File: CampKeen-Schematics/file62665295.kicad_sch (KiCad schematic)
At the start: 31 parts, among them Q10 2N7000, Q11 IRF9Z34NPBF, Q12 2N7000, Q13 2N7000, Q14 2N7000, Q15 2N7000, Q59 LTV-847

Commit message: working on input protection.
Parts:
- added R?: 1M, Resistor_THT:R_Axial_DIN0207_L6.3mm_D2.5mm_P2.54mm_Vertical, symbol Device:R
- Q59: footprint DIP762W60P254L1984H450Q16N -> SamacSys_Parts:DIP762W60P254L1984H450Q16N
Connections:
- net FullIN: now also R?.2; no longer Q14.2 (G), R47.1
- new net: Q14.2 (G), R47.1, R?.1
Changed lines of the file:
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@@
   (junction (at 158.75 153.67) (diameter 0) (color 0 0 0 0)
   )
+  (junction (at 144.78 134.62) (diameter 0) (color 0 0 0 0)
+  )
   (junction (at 68.58 20.32) (diameter 0) (color 0 0 0 0)
   )
@@
   (junction (at 116.84 96.52) (diameter 0) (color 0 0 0 0)
   )
-  (junction (at 144.78 134.62) (diameter 0) (color 0 0 0 0)
-  )
   (junction (at 40.64 52.07) (diameter 0) (color 0 0 0 0)
   )
@@
     (stroke (width 0) (type default) (color 0 0 0 0))
   )
-  (wire (pts (xy 134.62 134.62) (xy 144.78 134.62))
-    (stroke (width 0) (type default) (color 0 0 0 0))
-  )
   (wire (pts (xy 53.34 46.99) (xy 53.34 52.07))
     (stroke (width 0) (type default) (color 0 0 0 0))
@@
     (stroke (width 0) (type default) (color 0 0 0 0))
   )
+  (wire (pts (xy 134.62 134.62) (xy 135.89 134.62))
+    (stroke (width 0) (type default) (color 0 0 0 0))
+  )
   (wire (pts (xy 246.38 41.91) (xy 237.49 41.91))
     (stroke (width 0) (type default) (color 0 0 0 0))
   )
   (wire (pts (xy 144.78 149.86) (xy 144.78 153.67))
+    (stroke (width 0) (type default) (color 0 0 0 0))
+  )
+  (wire (pts (xy 143.51 134.62) (xy 144.78 134.62))
     (stroke (width 0) (type default) (color 0 0 0 0))
   )
@@
     (property "Reference" "Q59" (id 0) (at 207.01 30.099 0))
     (property "Value" "LTV-847" (id 1) (at 207.01 32.4104 0))
-    (property "Footprint" "DIP762W60P254L1984H450Q16N" (id 2) (at 224.79 34.29 0)
+    (property "Footprint" "SamacSys_Parts:DIP762W60P254L1984H450Q16N" (id 2) (at 224.79 34.29 0)
       (effects (font (size 1.27 1.27)) (justify left) hide)
     )
@@
       (effects (font (size 1.27 1.27)) hide)
     )
+    (pin "1")
+    (pin "2")
+  )
+  (symbol (lib_id "Device:R") (at 139.7 134.62 270)
+    (in_bom yes) (on_board yes)
+    (property "Reference" "R?" (id 0) (at 140.8684 136.398 0)
+      (effects (font (size 1.27 1.27)) (justify left))
+    )
+    (property "Value" "1M" (id 1) (at 138.557 136.398 0)
+      (effects (font (size 1.27 1.27)) (justify left))
+    )
+    (property "Footprint" "Resistor_THT:R_Axial_DIN0207_L6.3mm_D2.5mm_P2.54mm_Vertical" (id 2) (at 139.7 132.842 90)
+      (effects (font (size 1.27 1.27)) hide)
+    )
+    (property "Datasheet" "~" (id 3) (at 139.7 134.62 0)
+      (effects (font (size 1.27 1.27)) hide)
+    )

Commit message: work in progress for a design.
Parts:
- added R?: 220, Resistor_THT:R_Axial_DIN0207_L6.3mm_D2.5mm_P2.54mm_Vertical, symbol Device:R
- R47: value 1M -> 5K
- R?: value 1M -> 470
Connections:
- net FullIN: now also D12.1 (K), R47.1
- net at Q14.3 (D): now also R?.2; no longer D12.1 (K)
- net at D12.2 (A): now also Q14.2 (G), R?.1; no longer Q59.8 (CATHODE_4)
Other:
- moved on the sheet: C22, D12, Q14, R47, R?

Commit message: wip with changed values and delete of redundant resistor in new design
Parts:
- removed R?: 220, Resistor_THT:R_Axial_DIN0207_L6.3mm_D2.5mm_P2.54mm_Vertical, symbol Device:R
- renumbered C20 to C16, C21 to C17, C22 to C18, C23 to C19, D9 to D3, D10 to D6, D11 to D7, D12 to D8, Q10 to Q2, Q11 to Q3, Q12 to Q4, Q13 to Q5, Q59 to Q58, Q14 to Q6, Q15 to Q7, R40 to R15, R41 to R16, R42 to R17, R43 to R18, R44 to R19, R45 to R20, R46 to R21, R47 to R22, R48 to R23, R49 to R24, R50 to R25, R77 to R70, R78 to R71, R122 to R72, R123 to R76, Z3 to Z1
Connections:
- net FullIN: no longer R22.1
- net at D8.2 (A), Q6.2 (G), R?.1: now also R22.1
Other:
- moved on the sheet: C18, R22

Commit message: wip removing the traces fixing the inputs
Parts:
- removed C16, C17, C19: 22nF, Capacitor_THT:C_Disc_D4.7mm_W2.5mm_P5.00mm, symbol Device:C
- removed D3, D6, D7: 1N4007, Diode_THT:D_DO-41_SOD81_P10.16mm_Horizontal, symbol Diode:1N4007
- removed Q4, Q5, Q7: 2N7000, Package_TO_SOT_THT:TO-92_Inline, symbol Transistor_FET:2N7000
- removed R18, R19, R23: 1M, Resistor_THT:R_Axial_DIN0207_L6.3mm_D2.5mm_P2.54mm_Vertical, symbol Device:R
- removed R20, R21, R24, R25: 330, Resistor_THT:R_Axial_DIN0207_L6.3mm_D2.5mm_P2.54mm_Vertical, symbol Device:R
- removed R70, R71, R72, R76: 22k, Resistor_THT:R_Axial_DIN0207_L6.3mm_D2.5mm_P2.54mm_Vertical, symbol Device:R
- added C? (x3): 22nF, Capacitor_THT:C_Disc_D4.7mm_W2.5mm_P5.00mm, symbol Device:C
- added D? (x3): 1N4007, Diode_THT:D_DO-41_SOD81_P10.16mm_Horizontal, symbol Diode:1N4007
- added Q? (x3): 2N7000, Package_TO_SOT_THT:TO-92_Inline, symbol Transistor_FET:2N7000
- added R? (x3): 5K, Resistor_THT:R_Axial_DIN0207_L6.3mm_D2.5mm_P2.54mm_Vertical, symbol Device:R
- added R? (x3): 470, Resistor_THT:R_Axial_DIN0207_L6.3mm_D2.5mm_P2.54mm_Vertical, symbol Device:R
- added RN?: EXB-38V331JV, EXB38V472JV, symbol Samac_Sys:EXB-38V331JV
- added RN?: EXB-38V223JV, EXB38V472JV, symbol Samac_Sys:EXB-38V223JV
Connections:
- net +5V: now also RN?.5, RN?.5, RN?.6, RN?.6, RN?.7, RN?.7, RN?.8, RN?.8
- net 1-2IN: now also C?.1, D?.1 (K), R?.2
- net 1-2OUT: now also RN?.2
- net 1-4IN: now also C?.1, D?.1 (K), R?.2
- net 1-4OUT: now also RN?.1
- net 3-4IN: now also C?.1, D?.1 (K), R?.2
- net 3-4OUT: now also RN?.3
- net FullOUT: now also RN?.4
- net GND: now also C?.2, C?.2, C?.2, Q?.1 (S), Q?.1 (S), Q?.1 (S), R?.2, R?.2, R?.2
- net at Q58.2 (CATHODE_1): now also Q?.3 (D)
- net at Q58.4 (CATHODE_2): now also Q?.3 (D)
- net at Q58.6 (CATHODE_3): now also Q?.3 (D)
- net at Q58.1 (ANODE_1): now also RN?.4
- net at Q58.3 (ANODE_2): now also RN?.3
- net at Q58.5 (ANODE_3): now also RN?.2
- net at Q58.7 (ANODE_4): now also RN?.1
- net at Q58.8 (CATHODE_4): now also Q6.3 (D)
- new net: D?.2 (A), Q?.2 (G), R?.1, R?.1 (x3)
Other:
- moved on the sheet: C18, D8, Q58, Q6, R22, R?

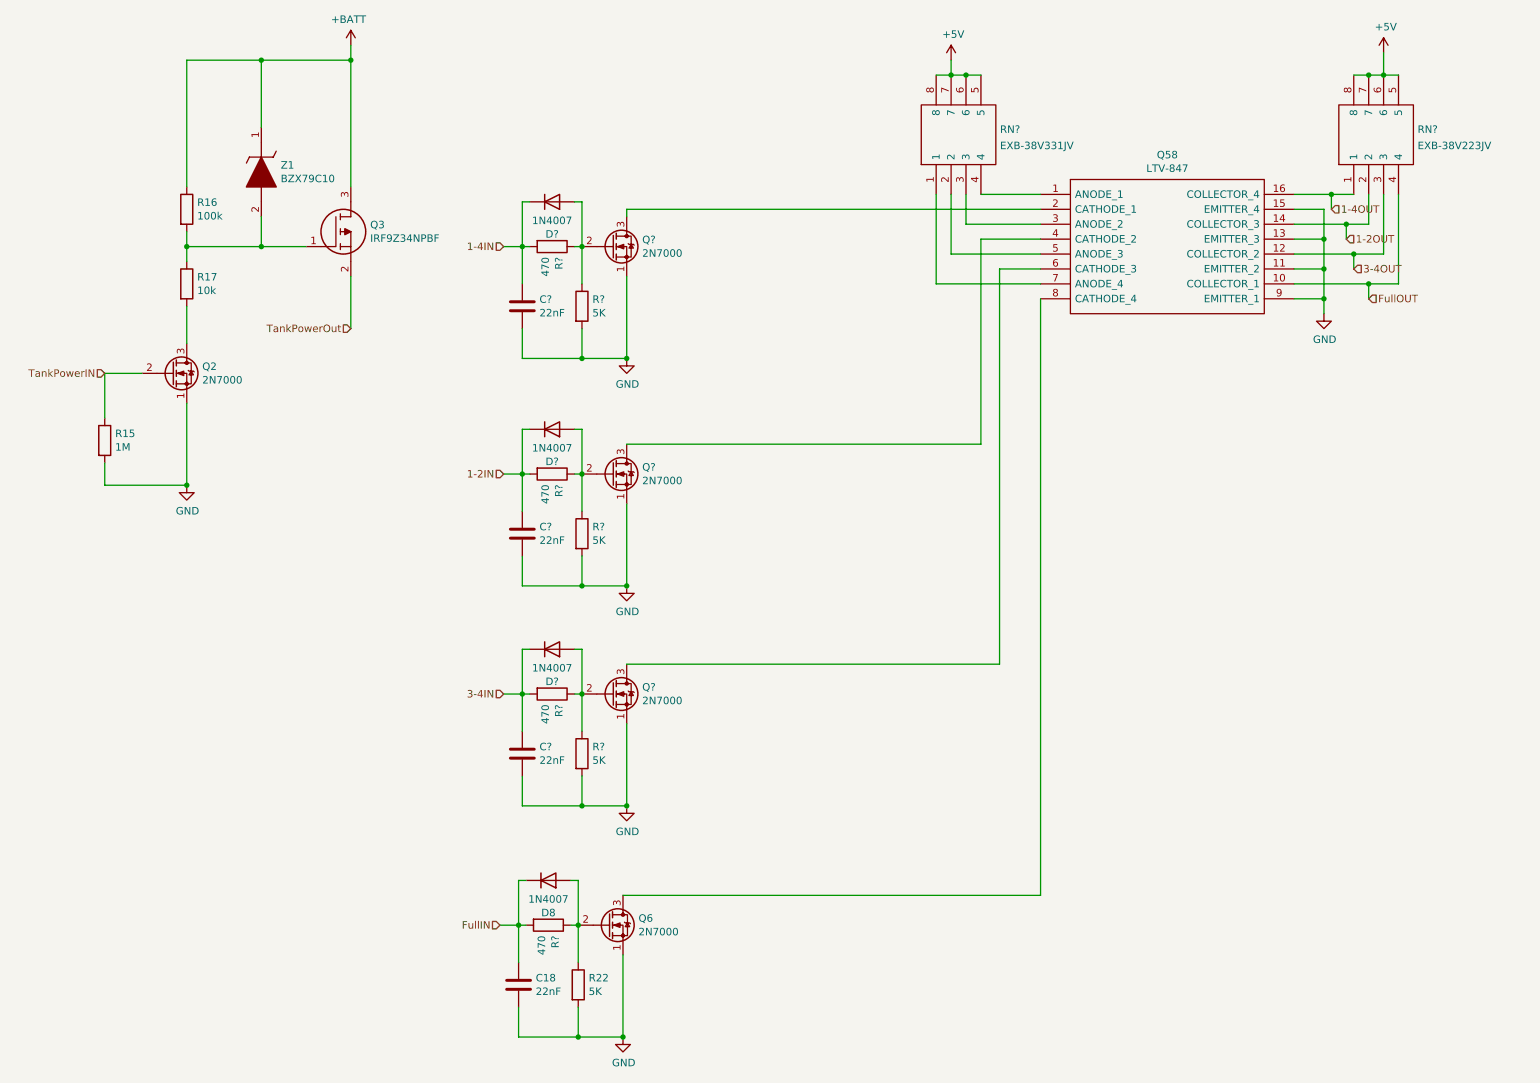
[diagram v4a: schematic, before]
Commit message: adding in 3.3v 3A for the ESP32
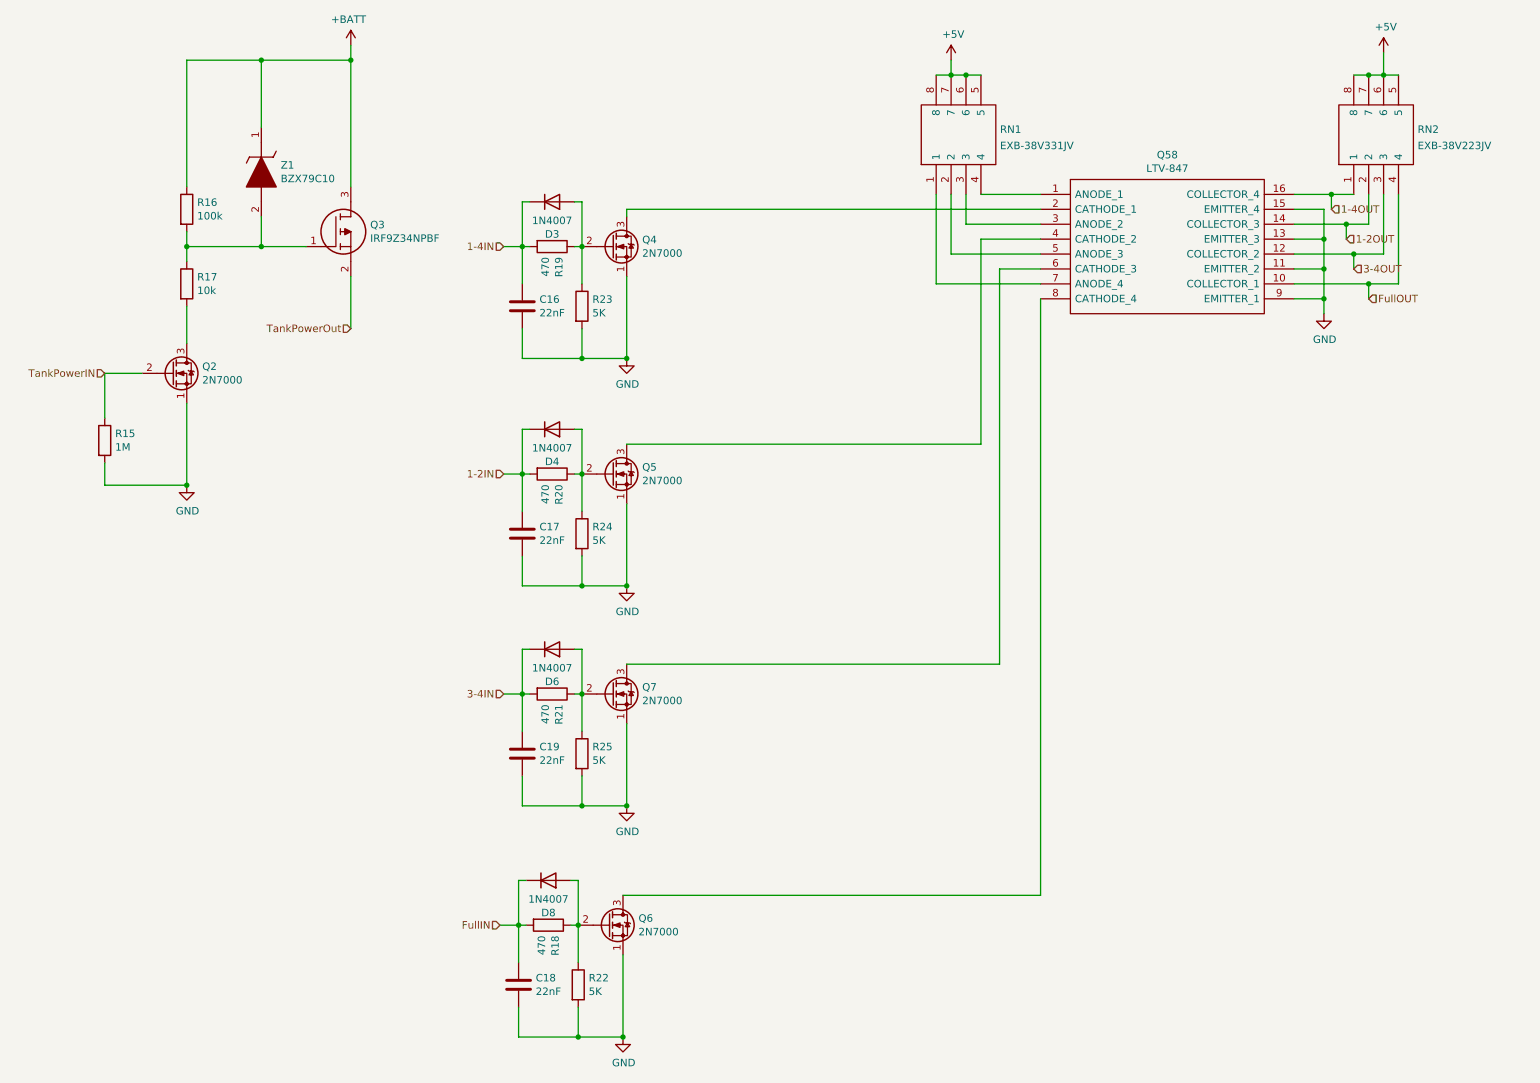
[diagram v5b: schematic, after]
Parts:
- gave numbers to parts that had none: 18
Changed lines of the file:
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@@
   (symbol (lib_id "power:GND") (at 234.315 63.5 0)
     (in_bom yes) (on_board yes)
-    (property "Reference" "#PWR0154" (id 0) (at 234.315 69.85 0)
+    (property "Reference" "#PWR0159" (id 0) (at 234.315 69.85 0)
       (effects (font (size 1.27 1.27)) hide)
     )
@@
   (symbol (lib_id "power:+5V") (at 244.475 19.05 0)
     (in_bom yes) (on_board yes)
-    (property "Reference" "#PWR0158" (id 0) (at 244.475 22.86 0)
+    (property "Reference" "#PWR0163" (id 0) (at 244.475 22.86 0)
       (effects (font (size 1.27 1.27)) hide)
     )
@@
   (symbol (lib_id "power:+5V") (at 170.815 20.32 0)
     (in_bom yes) (on_board yes)
-    (property "Reference" "#PWR066" (id 0) (at 170.815 24.13 0)
+    (property "Reference" "#PWR089" (id 0) (at 170.815 24.13 0)
       (effects (font (size 1.27 1.27)) hide)
     )
@@
   (symbol (lib_id "power:+BATT") (at 68.58 17.78 0) (mirror y)
     (in_bom yes) (on_board yes)
-    (property "Reference" "#PWR065" (id 0) (at 68.58 21.59 0)
+    (property "Reference" "#PWR088" (id 0) (at 68.58 21.59 0)
       (effects (font (size 1.27 1.27)) hide)
     )
@@
   (symbol (lib_id "power:GND") (at 40.64 92.71 0)
     (in_bom yes) (on_board yes)
-    (property "Reference" "#PWR064" (id 0) (at 40.64 99.06 0)
+    (property "Reference" "#PWR087" (id 0) (at 40.64 99.06 0)
       (effects (font (size 1.27 1.27)) hide)
     )
@@
   (symbol (lib_id "power:GND") (at 114.935 186.69 0)
     (in_bom yes) (on_board yes)
-    (property "Reference" "#PWR071" (id 0) (at 114.935 193.04 0)
+    (property "Reference" "#PWR094" (id 0) (at 114.935 193.04 0)
       (effects (font (size 1.27 1.27)) hide)
     )
@@
   (symbol (lib_id "Device:C") (at 97.79 138.43 0)
     (in_bom yes) (on_board yes)
-    (property "Reference" "C?" (id 0) (at 100.711 137.2616 0)
+    (property "Reference" "C19" (id 0) (at 100.711 137.2616 0)
       (effects (font (size 1.27 1.27)) (justify left))
     )
@@
   (symbol (lib_id "Diode:1N4007") (at 102.87 83.185 0) (mirror x)
     (in_bom yes) (on_board yes)
-    (property "Reference" "D?" (id 0) (at 102.87 88.6968 0))
+    (property "Reference" "D4" (id 0) (at 102.87 88.6968 0))
     (property "Value" "1N4007" (id 1) (at 102.87 86.3854 0))
     (property "Footprint" "Diode_THT:D_DO-41_SOD81_P10.16mm_Horizontal" (id 2) (at 102.87 78.74 0)
@@
   (symbol (lib_id "Device:C") (at 97.79 62.23 0)
     (in_bom yes) (on_board yes)
-    (property "Reference" "C?" (id 0) (at 100.711 61.0616 0)
+    (property "Reference" "C16" (id 0) (at 100.711 61.0616 0)
       (effects (font (size 1.27 1.27)) (justify left))
     )
@@
   (symbol (lib_id "power:GND") (at 115.57 109.855 0)
     (in_bom yes) (on_board yes)
-    (property "Reference" "#PWR?" (id 0) (at 115.57 116.205 0)
+    (property "Reference" "#PWR073" (id 0) (at 115.57 116.205 0)
       (effects (font (size 1.27 1.27)) hide)
     )
@@
   (symbol (lib_id "Transistor_FET:2N7000") (at 113.03 52.07 0)
     (in_bom yes) (on_board yes)
-    (property "Reference" "Q?" (id 0) (at 118.2116 50.9016 0)
+    (property "Reference" "Q4" (id 0) (at 118.2116 50.9016 0)
       (effects (font (size 1.27 1.27)) (justify left))
     )
@@
   (symbol (lib_id "Device:R") (at 107.95 138.43 0)
     (in_bom yes) (on_board yes)
-    (property "Reference" "R?" (id 0) (at 109.728 137.2616 0)
+    (property "Reference" "R25" (id 0) (at 109.728 137.2616 0)
       (effects (font (size 1.27 1.27)) (justify left))
     )
@@
   (symbol (lib_id "Samac_Sys:EXB-38V331JV") (at 168.275 43.18 90)
     (in_bom yes) (on_board yes) (fields_autoplaced)
-    (property "Reference" "RN?" (id 0) (at 179.1462 32.1115 90)
+    (property "Reference" "RN1" (id 0) (at 179.1462 32.1115 90)
       (effects (font (size 1.27 1.27)) (justify right))
     )
@@
   (symbol (lib_id "Device:C") (at 97.79 100.965 0)
     (in_bom yes) (on_board yes)
-    (property "Reference" "C?" (id 0) (at 100.711 99.7966 0)
+    (property "Reference" "C17" (id 0) (at 100.711 99.7966 0)
       (effects (font (size 1.27 1.27)) (justify left))
     )
@@
   (symbol (lib_id "Device:R") (at 107.95 100.965 0)
     (in_bom yes) (on_board yes)
-    (property "Reference" "R?" (id 0) (at 109.728 99.7966 0)
+    (property "Reference" "R24" (id 0) (at 109.728 99.7966 0)
       (effects (font (size 1.27 1.27)) (justify left))
     )
@@
   (symbol (lib_id "Diode:1N4007") (at 102.87 120.65 0) (mirror x)
     (in_bom yes) (on_board yes)
-    (property "Reference" "D?" (id 0) (at 102.87 126.1618 0))
+    (property "Reference" "D6" (id 0) (at 102.87 126.1618 0))
     (property "Value" "1N4007" (id 1) (at 102.87 123.8504 0))
     (property "Footprint" "Diode_THT:D_DO-41_SOD81_P10.16mm_Horizontal" (id 2) (at 102.87 116.205 0)
@@
   (symbol (lib_id "Device:R") (at 107.95 62.23 0)
     (in_bom yes) (on_board yes)
-    (property "Reference" "R?" (id 0) (at 109.728 61.0616 0)
+    (property "Reference" "R23" (id 0) (at 109.728 61.0616 0)
       (effects (font (size 1.27 1.27)) (justify left))
     )
@@
   (symbol (lib_id "Transistor_FET:2N7000") (at 113.03 128.27 0)
     (in_bom yes) (on_board yes)
-    (property "Reference" "Q?" (id 0) (at 118.2116 127.1016 0)
+    (property "Reference" "Q7" (id 0) (at 118.2116 127.1016 0)
       (effects (font (size 1.27 1.27)) (justify left))
     )
@@
   (symbol (lib_id "Device:R") (at 102.87 90.805 270)
     (in_bom yes) (on_board yes)
-    (property "Reference" "R?" (id 0) (at 104.0384 92.583 0)
+    (property "Reference" "R20" (id 0) (at 104.0384 92.583 0)
       (effects (font (size 1.27 1.27)) (justify left))
     )
@@
   (symbol (lib_id "power:GND") (at 115.57 71.12 0)
     (in_bom yes) (on_board yes)
-    (property "Reference" "#PWR?" (id 0) (at 115.57 77.47 0)
+    (property "Reference" "#PWR072" (id 0) (at 115.57 77.47 0)
       (effects (font (size 1.27 1.27)) hide)
     )
@@
   (symbol (lib_id "Diode:1N4007") (at 102.87 44.45 0) (mirror x)
     (in_bom yes) (on_board yes)
-    (property "Reference" "D?" (id 0) (at 102.87 49.9618 0))
+    (property "Reference" "D3" (id 0) (at 102.87 49.9618 0))
     (property "Value" "1N4007" (id 1) (at 102.87 47.6504 0))
     (property "Footprint" "Diode_THT:D_DO-41_SOD81_P10.16mm_Horizontal" (id 2) (at 102.87 40.005 0)
@@
   (symbol (lib_id "Samac_Sys:EXB-38V223JV") (at 239.395 43.18 90)
     (in_bom yes) (on_board yes) (fields_autoplaced)
-    (property "Reference" "RN?" (id 0) (at 250.2662 32.1115 90)
+    (property "Reference" "RN2" (id 0) (at 250.2662 32.1115 90)
       (effects (font (size 1.27 1.27)) (justify right))
     )
@@
   (symbol (lib_id "Device:R") (at 102.87 128.27 270)
     (in_bom yes) (on_board yes)
-    (property "Reference" "R?" (id 0) (at 104.0384 130.048 0)
+    (property "Reference" "R21" (id 0) (at 104.0384 130.048 0)
       (effects (font (size 1.27 1.27)) (justify left))
     )
@@
   (symbol (lib_id "Transistor_FET:2N7000") (at 113.03 90.805 0)
     (in_bom yes) (on_board yes)
-    (property "Reference" "Q?" (id 0) (at 118.2116 89.6366 0)
+    (property "Reference" "Q5" (id 0) (at 118.2116 89.6366 0)
       (effects (font (size 1.27 1.27)) (justify left))
     )
@@
   (symbol (lib_id "Device:R") (at 102.235 167.64 270)
     (in_bom yes) (on_board yes)
-    (property "Reference" "R?" (id 0) (at 103.4034 169.418 0)
+    (property "Reference" "R18" (id 0) (at 103.4034 169.418 0)
       (effects (font (size 1.27 1.27)) (justify left))
     )
@@
   (symbol (lib_id "power:GND") (at 115.57 147.32 0)
     (in_bom yes) (on_board yes)
-    (property "Reference" "#PWR?" (id 0) (at 115.57 153.67 0)
+    (property "Reference" "#PWR090" (id 0) (at 115.57 153.67 0)
       (effects (font (size 1.27 1.27)) hide)
     )
@@
   (symbol (lib_id "Device:R") (at 102.87 52.07 270)
     (in_bom yes) (on_board yes)
-    (property "Reference" "R?" (id 0) (at 104.0384 53.848 0)
-      (effects (font (size 1.27 1.27)) (justify left))
-    )
+    (property "Reference" "R19" (id 0) (at 104.0384 53.848 0)
+      (effects (font (size 1.27 1.27)) (justify left))
+    )
